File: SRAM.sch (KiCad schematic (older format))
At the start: 5 parts

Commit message: Merged 8254
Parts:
- gave numbers to parts that had none: 5
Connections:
- net BHE': now also U12.6 (I6); no longer U12.3 (I3)
- net M-IO': now also U12.7 (I7); no longer U12.4 (I4)
- net A19: now reaches U12.5 (I5)
- new net A17: U12.3 (I3)
- new net A18: U12.4 (I4)
- no-connect marks 10 -> 7
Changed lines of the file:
@@
 $Descr A4 11693 8268
 encoding utf-8
-Sheet 2 6
+Sheet 6 8
 Title ""
 Date ""
@@
 	3300 1700 3200 1700
 $Comp
-L Memory_RAM:CY7C199 U?
+L Memory_RAM:CY7C199 U13
 U 1 1 61BF2207
 P 3900 2600
-F 0 "U?" H 3900 3981 50  0000 C CNN
+F 0 "U13" H 3900 3981 50  0000 C CNN
 F 1 "CY7C199" H 3900 3890 50  0000 C CNN
 F 2 "" H 3900 2600 50  0001 C CNN
@@
 Wire Wire Line
 	3000 3500 3300 3500
-Wire Wire Line
-	1400 4000 1700 4000
 Text Notes 4600 1250 0    50   ~ 0
 Upper (ODD) Bank\n
 Text Notes 4550 7150 0    50   ~ 0
 Lower (Even) Bank\n
-$Comp
-L Logic_Programmable:PAL16L8 U?
-U 1 1 61C00AE8
-P 2200 4300
-F 0 "U?" H 2200 5181 50  0000 C CNN
-F 1 "PAL16L8" H 2200 5090 50  0000 C CNN
-F 2 "" H 2200 4300 50  0001 C CNN
-F 3 "" H 2200 4300 50  0001 C CNN
-	1    2200 4300
-	1    0    0    -1
-$EndComp
 Wire Wire Line
 	2700 3300 3300 3300
@@
 Wire Wire Line
 	1300 1400 1200 1400
-Wire Wire Line
-	1300 4100 1700 4100
-$Comp
-L power:GND #PWR?
+$Comp
+L power:GND #PWR0160
 U 1 1 61D25220
 P 3900 3800
-F 0 "#PWR?" H 3900 3550 50  0001 C CNN
+F 0 "#PWR0160" H 3900 3550 50  0001 C CNN
 F 1 "GND" H 3905 3627 50  0000 C CNN
 F 2 "" H 3900 3800 50  0001 C CNN
@@
 $EndComp
 $Comp
-L power:+5V #PWR?
+L power:+5V #PWR0161
 U 1 1 61D254C1
 P 3900 1400
-F 0 "#PWR?" H 3900 1250 50  0001 C CNN
+F 0 "#PWR0161" H 3900 1250 50  0001 C CNN
 F 1 "+5V" V 3915 1528 50  0000 L CNN
 F 2 "" H 3900 1400 50  0001 C CNN
@@
 $EndComp
 $Comp
-L power:+5V #PWR?
+L power:+5V #PWR0162
 U 1 1 61D260A2
 P 2200 3600
-F 0 "#PWR?" H 2200 3450 50  0001 C CNN
+F 0 "#PWR0162" H 2200 3450 50  0001 C CNN
 F 1 "+5V" V 2215 3728 50  0000 L CNN
 F 2 "" H 2200 3600 50  0001 C CNN
@@
 $EndComp
 $Comp
-L power:GND #PWR?
+L power:GND #PWR0163
 U 1 1 61D263BA
 P 2200 4900
-F 0 "#PWR?" H 2200 4650 50  0001 C CNN
+F 0 "#PWR0163" H 2200 4650 50  0001 C CNN
 F 1 "GND" H 2205 4727 50  0000 C CNN
 F 2 "" H 2200 4900 50  0001 C CNN
@@
 NoConn ~ 2700 4400
 NoConn ~ 2700 4500
-NoConn ~ 1700 4200
-NoConn ~ 1700 4300
-NoConn ~ 1700 4400
-NoConn ~ 1700 4500
 NoConn ~ 1700 4600
 NoConn ~ 1700 4700
@@
 	3300 4700 3200 4700
 $Comp
-L Memory_RAM:CY7C199 U?
+L Memory_RAM:CY7C199 U14
 U 1 1 61D93083
 P 3900 5600
-F 0 "U?" H 3900 6981 50  0000 C CNN
+F 0 "U14" H 3900 6981 50  0000 C CNN
 F 1 "CY7C199" H 3900 6890 50  0000 C CNN
 F 2 "" H 3900 5600 50  0001 C CNN
@@
 	3000 6500 3300 6500
 $Comp
-L power:GND #PWR?
+L power:GND #PWR0164
 U 1 1 61D930C9
 P 3900 6800
-F 0 "#PWR?" H 3900 6550 50  0001 C CNN
+F 0 "#PWR0164" H 3900 6550 50  0001 C CNN
 F 1 "GND" H 3905 6627 50  0000 C CNN
 F 2 "" H 3900 6800 50  0001 C CNN
@@
 $EndComp
 $Comp
-L power:+5V #PWR?
+L power:+5V #PWR0165
 U 1 1 61D930D3
 P 3900 4400
-F 0 "#PWR?" H 3900 4250 50  0001 C CNN
+F 0 "#PWR0165" H 3900 4250 50  0001 C CNN
 F 1 "+5V" V 3915 4528 50  0000 L CNN
 F 2 "" H 3900 4400 50  0001 C CNN
@@
 	5500 4700 5400 4700
 $Comp
-L Memory_RAM:CY7C199 U?
+L Memory_RAM:CY7C199 U16
 U 1 1 61DCF4EE
 P 6100 5600
-F 0 "U?" H 6100 6981 50  0000 C CNN
+F 0 "U16" H 6100 6981 50  0000 C CNN
 F 1 "CY7C199" H 6100 6890 50  0000 C CNN
 F 2 "" H 6100 5600 50  0001 C CNN
@@
 	4900 6300 5500 6300
 $Comp
-L power:GND #PWR?
+L power:GND #PWR0166
 U 1 1 61DCF52C
 P 6100 6800
-F 0 "#PWR?" H 6100 6550 50  0001 C CNN
+F 0 "#PWR0166" H 6100 6550 50  0001 C CNN
 F 1 "GND" H 6105 6627 50  0000 C CNN
 F 2 "" H 6100 6800 50  0001 C CNN
@@
 $EndComp
 $Comp
-L power:+5V #PWR?
+L power:+5V #PWR0167
 U 1 1 61DCF532
 P 6100 4400
-F 0 "#PWR?" H 6100 4250 50  0001 C CNN
+F 0 "#PWR0167" H 6100 4250 50  0001 C CNN
 F 1 "+5V" V 6115 4528 50  0000 L CNN
 F 2 "" H 6100 4400 50  0001 C CNN
@@
 	5500 1700 5400 1700
 $Comp
-L Memory_RAM:CY7C199 U?
+L Memory_RAM:CY7C199 U15
 U 1 1 61DD75B1
 P 6100 2600
-F 0 "U?" H 6100 3981 50  0000 C CNN
+F 0 "U15" H 6100 3981 50  0000 C CNN
 F 1 "CY7C199" H 6100 3890 50  0000 C CNN
 F 2 "" H 6100 2600 50  0001 C CNN
@@
 	4900 3300 5500 3300
 $Comp
-L power:GND #PWR?
+L power:GND #PWR0168
 U 1 1 61DD75EF
 P 6100 3800
-F 0 "#PWR?" H 6100 3550 50  0001 C CNN
+F 0 "#PWR0168" H 6100 3550 50  0001 C CNN
 F 1 "GND" H 6105 3627 50  0000 C CNN
 F 2 "" H 6100 3800 50  0001 C CNN
@@
 $EndComp
 $Comp
-L power:+5V #PWR?
+L power:+5V #PWR0169
 U 1 1 61DD75F5
 P 6100 1400
-F 0 "#PWR?" H 6100 1250 50  0001 C CNN
+F 0 "#PWR0169" H 6100 1250 50  0001 C CNN
 F 1 "+5V" V 6115 1528 50  0000 L CNN
 F 2 "" H 6100 1400 50  0001 C CNN
@@
 OE'
 Wire Wire Line
-	1300 1400 1300 4100
-Wire Wire Line
-	1400 1300 1400 4000
+	1300 1400 1300 4400
+Wire Wire Line
+	1400 1300 1400 4300
 Wire Wire Line
 	1200 1300 1400 1300
@@
 Text Label 6700 5400 0    50   ~ 0
 D7
+$Comp
+L Logic_Programmable:PAL16L8 U12
+U 1 1 61C00AE8
+P 2200 4300
+F 0 "U12" H 2200 5181 50  0000 C CNN
+F 1 "PAL16L8" H 2200 5090 50  0000 C CNN
+F 2 "" H 2200 4300 50  0001 C CNN
+F 3 "" H 2200 4300 50  0001 C CNN
+	1    2200 4300
+	1    0    0    -1
+$EndComp
+Wire Wire Line
+	1700 4000 1600 4000
+Wire Wire Line
+	1700 4100 1600 4100
+Wire Wire Line
+	1700 4200 1600 4200
+Entry Wire Line
+	1500 3900 1600 4000
+Entry Wire Line
+	1500 4000 1600 4100
+Entry Wire Line
+	1500 4100 1600 4200
+Text Label 1600 4000 0    50   ~ 0
+A17
+Text Label 1600 4100 0    50   ~ 0
+A18
+Text Label 1600 4200 0    50   ~ 0
+A19
+Wire Wire Line
+	1400 4300 1700 4300
+Wire Wire Line
+	1300 4400 1700 4400
+NoConn ~ 1700 4500
 Wire Bus Line
-	1500 1000 1500 3800
+	1500 1000 1500 4100
 Wire Bus Line
 	6900 1800 6900 4100

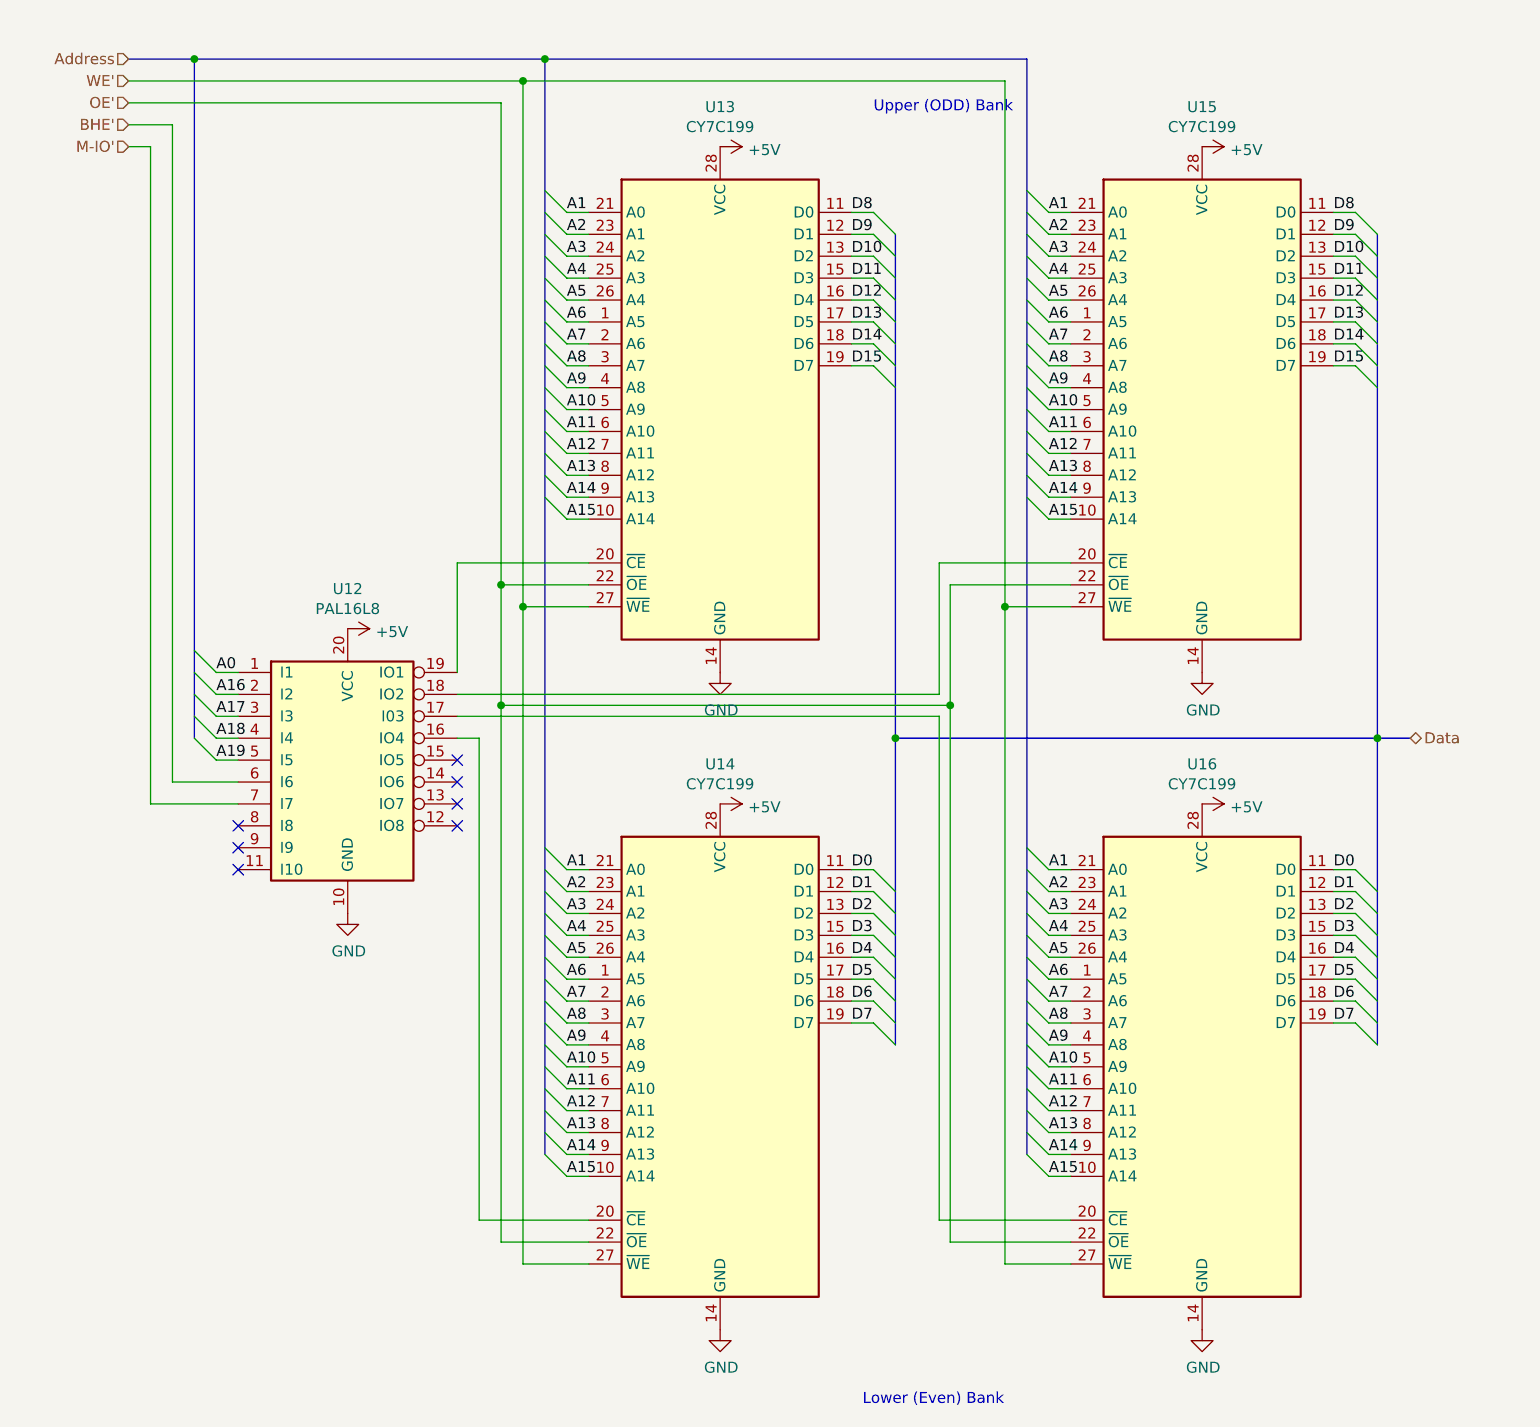
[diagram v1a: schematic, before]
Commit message: Integrated LCD.  Fixed issues with busses
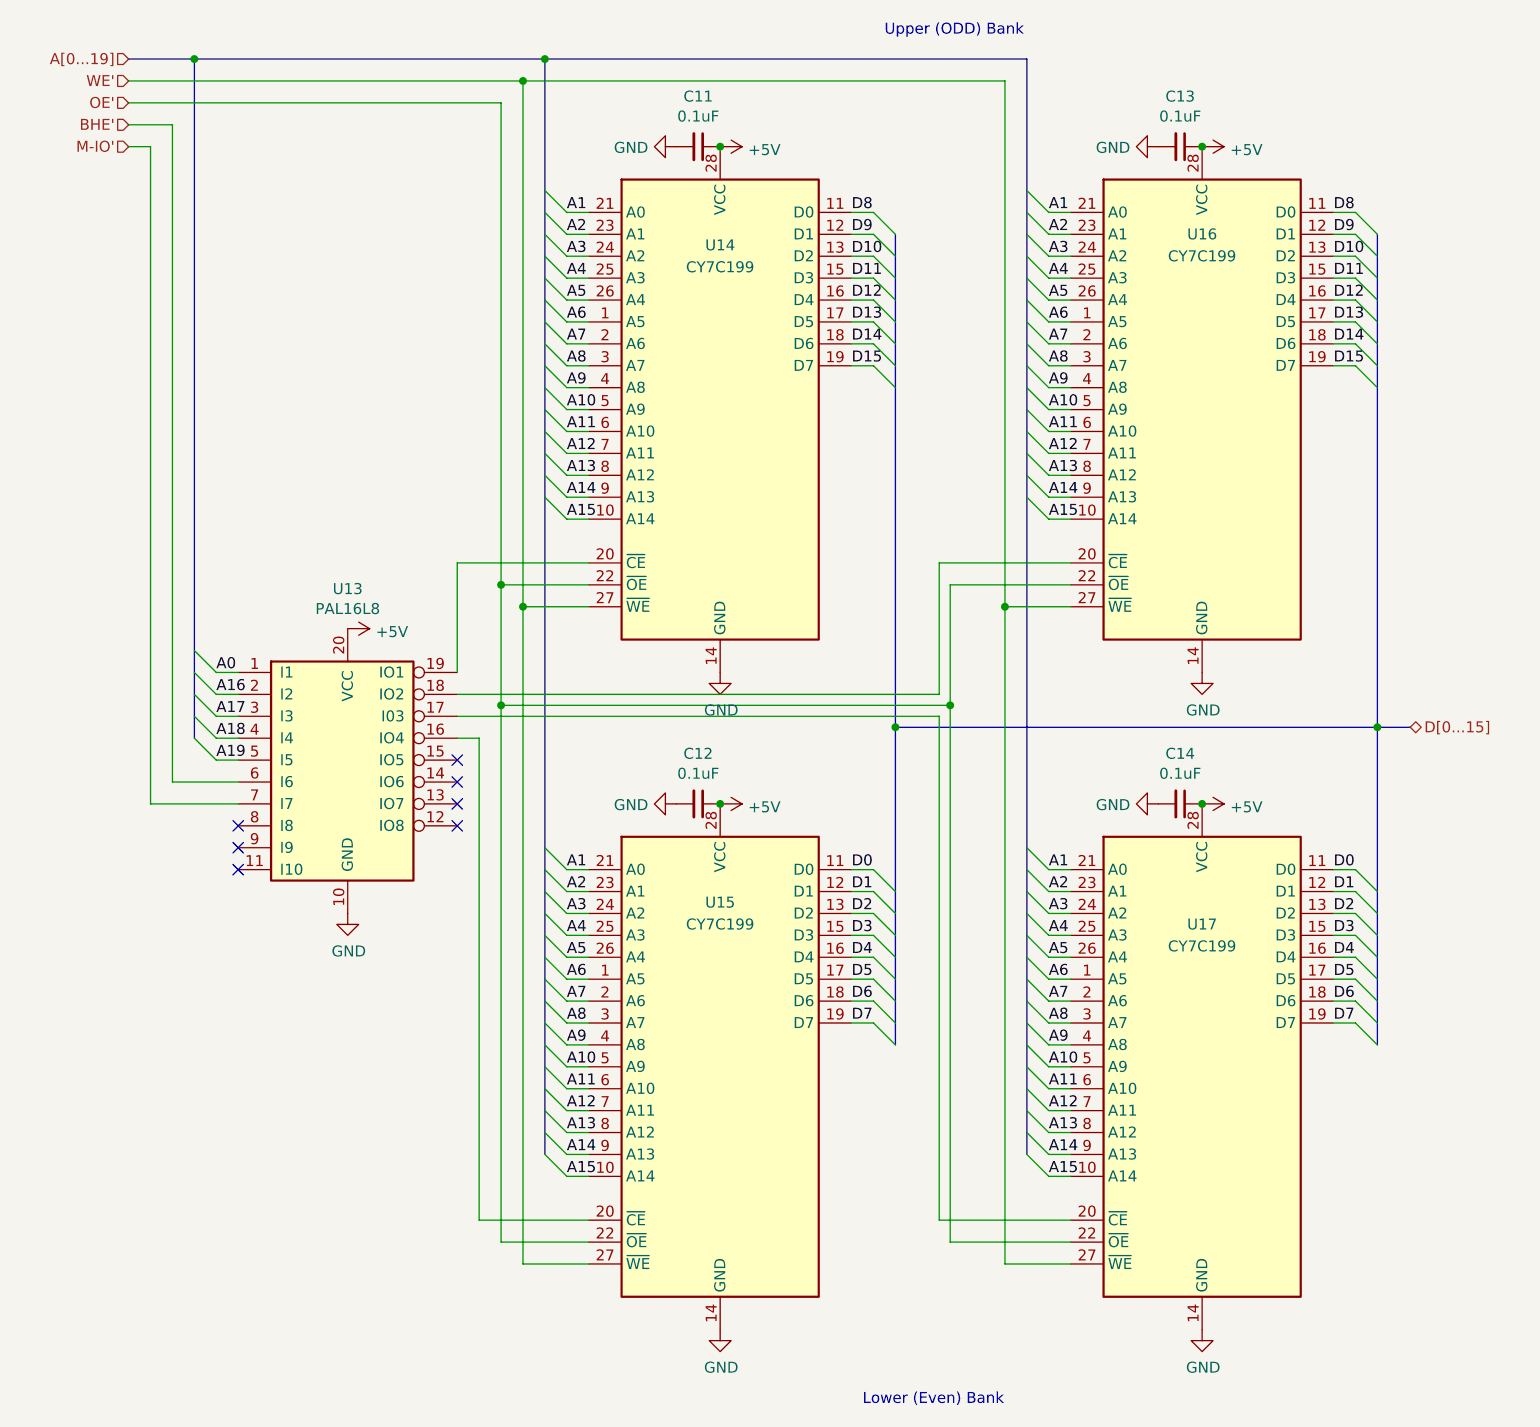
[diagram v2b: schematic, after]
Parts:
- added C11, C12, C13, C14: 0.1uF, symbol Device:C_Small
- renumbered U12 to U13, U13 to U14, U14 to U15, U15 to U16, U16 to U17
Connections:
- net +5V: now also C11.1, C12.1, C13.1, C14.1
- net GND: now also C11.2, C12.2, C13.2, C14.2
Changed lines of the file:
@@
 $Descr A4 11693 8268
 encoding utf-8
-Sheet 6 8
+Sheet 6 9
 Title ""
 Date ""
@@
 	3300 1700 3200 1700
 $Comp
-L Memory_RAM:CY7C199 U13
+L Memory_RAM:CY7C199 U14
 U 1 1 61BF2207
 P 3900 2600
-F 0 "U13" H 3900 3981 50  0000 C CNN
-F 1 "CY7C199" H 3900 3890 50  0000 C CNN
+F 0 "U14" H 3900 3350 50  0000 C CNN
+F 1 "CY7C199" H 3900 3250 50  0000 C CNN
 F 2 "" H 3900 2600 50  0001 C CNN
 F 3 "" H 3900 2600 50  0001 C CNN
@@
 Wire Wire Line
 	3000 3500 3300 3500
-Text Notes 4600 1250 0    50   ~ 0
+Text Notes 4650 900  0    50   ~ 0
 Upper (ODD) Bank\n
 Text Notes 4550 7150 0    50   ~ 0
@@
 	1200 1000 1500 1000
 Text HLabel 1200 1000 0    50   Input ~ 0
-Address
+A[0...19]
 Text HLabel 1200 1400 0    50   Input ~ 0
 M-IO'
@@
 	1300 1400 1200 1400
 $Comp
-L power:GND #PWR0160
+L power:GND #PWR074
 U 1 1 61D25220
 P 3900 3800
-F 0 "#PWR0160" H 3900 3550 50  0001 C CNN
+F 0 "#PWR074" H 3900 3550 50  0001 C CNN
 F 1 "GND" H 3905 3627 50  0000 C CNN
 F 2 "" H 3900 3800 50  0001 C CNN
@@
 $EndComp
 $Comp
-L power:+5V #PWR0161
+L power:+5V #PWR073
 U 1 1 61D254C1
 P 3900 1400
-F 0 "#PWR0161" H 3900 1250 50  0001 C CNN
+F 0 "#PWR073" H 3900 1250 50  0001 C CNN
 F 1 "+5V" V 3915 1528 50  0000 L CNN
 F 2 "" H 3900 1400 50  0001 C CNN
@@
 $EndComp
 $Comp
-L power:+5V #PWR0162
+L power:+5V #PWR069
 U 1 1 61D260A2
 P 2200 3600
-F 0 "#PWR0162" H 2200 3450 50  0001 C CNN
+F 0 "#PWR069" H 2200 3450 50  0001 C CNN
 F 1 "+5V" V 2215 3728 50  0000 L CNN
 F 2 "" H 2200 3600 50  0001 C CNN
@@
 $EndComp
 $Comp
-L power:GND #PWR0163
+L power:GND #PWR070
 U 1 1 61D263BA
 P 2200 4900
-F 0 "#PWR0163" H 2200 4650 50  0001 C CNN
+F 0 "#PWR070" H 2200 4650 50  0001 C CNN
 F 1 "GND" H 2205 4727 50  0000 C CNN
 F 2 "" H 2200 4900 50  0001 C CNN
@@
 	3300 4700 3200 4700
 $Comp
-L Memory_RAM:CY7C199 U14
+L Memory_RAM:CY7C199 U15
 U 1 1 61D93083
 P 3900 5600
-F 0 "U14" H 3900 6981 50  0000 C CNN
-F 1 "CY7C199" H 3900 6890 50  0000 C CNN
+F 0 "U15" H 3900 6350 50  0000 C CNN
+F 1 "CY7C199" H 3900 6250 50  0000 C CNN
 F 2 "" H 3900 5600 50  0001 C CNN
 F 3 "" H 3900 5600 50  0001 C CNN
@@
 	3000 6500 3300 6500
 $Comp
-L power:GND #PWR0164
+L power:GND #PWR076
 U 1 1 61D930C9
 P 3900 6800
-F 0 "#PWR0164" H 3900 6550 50  0001 C CNN
+F 0 "#PWR076" H 3900 6550 50  0001 C CNN
 F 1 "GND" H 3905 6627 50  0000 C CNN
 F 2 "" H 3900 6800 50  0001 C CNN
@@
 $EndComp
 $Comp
-L power:+5V #PWR0165
+L power:+5V #PWR075
 U 1 1 61D930D3
 P 3900 4400
-F 0 "#PWR0165" H 3900 4250 50  0001 C CNN
+F 0 "#PWR075" H 3900 4250 50  0001 C CNN
 F 1 "+5V" V 3915 4528 50  0000 L CNN
 F 2 "" H 3900 4400 50  0001 C CNN
@@
 Wire Wire Line
 	5500 4700 5400 4700
-$Comp
-L Memory_RAM:CY7C199 U16
-U 1 1 61DCF4EE
-P 6100 5600
-F 0 "U16" H 6100 6981 50  0000 C CNN
-F 1 "CY7C199" H 6100 6890 50  0000 C CNN
-F 2 "" H 6100 5600 50  0001 C CNN
-F 3 "" H 6100 5600 50  0001 C CNN
-	1    6100 5600
-	1    0    0    -1
-$EndComp
 Wire Wire Line
 	6700 4700 6800 4700
@@
 	4900 6300 5500 6300
 $Comp
-L power:GND #PWR0166
+L power:GND #PWR082
 U 1 1 61DCF52C
 P 6100 6800
-F 0 "#PWR0166" H 6100 6550 50  0001 C CNN
+F 0 "#PWR082" H 6100 6550 50  0001 C CNN
 F 1 "GND" H 6105 6627 50  0000 C CNN
 F 2 "" H 6100 6800 50  0001 C CNN
@@
 $EndComp
 $Comp
-L power:+5V #PWR0167
+L power:+5V #PWR081
 U 1 1 61DCF532
 P 6100 4400
-F 0 "#PWR0167" H 6100 4250 50  0001 C CNN
+F 0 "#PWR081" H 6100 4250 50  0001 C CNN
 F 1 "+5V" V 6115 4528 50  0000 L CNN
 F 2 "" H 6100 4400 50  0001 C CNN
@@
 	5500 1700 5400 1700
 $Comp
-L Memory_RAM:CY7C199 U15
+L Memory_RAM:CY7C199 U16
 U 1 1 61DD75B1
 P 6100 2600
-F 0 "U15" H 6100 3981 50  0000 C CNN
-F 1 "CY7C199" H 6100 3890 50  0000 C CNN
+F 0 "U16" H 6100 3400 50  0000 C CNN
+F 1 "CY7C199" H 6100 3300 50  0000 C CNN
 F 2 "" H 6100 2600 50  0001 C CNN
 F 3 "" H 6100 2600 50  0001 C CNN
@@
 	4900 3300 5500 3300
 $Comp
-L power:GND #PWR0168
+L power:GND #PWR080
 U 1 1 61DD75EF
 P 6100 3800
-F 0 "#PWR0168" H 6100 3550 50  0001 C CNN
+F 0 "#PWR080" H 6100 3550 50  0001 C CNN
 F 1 "GND" H 6105 3627 50  0000 C CNN
 F 2 "" H 6100 3800 50  0001 C CNN
@@
 $EndComp
 $Comp
-L power:+5V #PWR0169
+L power:+5V #PWR079
 U 1 1 61DD75F5
 P 6100 1400
-F 0 "#PWR0169" H 6100 1250 50  0001 C CNN
+F 0 "#PWR079" H 6100 1250 50  0001 C CNN
 F 1 "+5V" V 6115 1528 50  0000 L CNN
 F 2 "" H 6100 1400 50  0001 C CNN
@@
 Connection ~ 3100 1000
 Wire Bus Line
-	4700 4100 6900 4100
-Connection ~ 4700 4100
-Connection ~ 6900 4100
-Wire Bus Line
-	6900 4100 7050 4100
-Text HLabel 7050 4100 2    50   BiDi ~ 0
-Data
+	4700 4050 6900 4050
+Connection ~ 4700 4050
+Connection ~ 6900 4050
+Wire Bus Line
+	6900 4050 7050 4050
+Text HLabel 7050 4050 2    50   BiDi ~ 0
+D[0...15]
 Wire Wire Line
 	2700 3900 4900 3900
@@
 D7
 $Comp
-L Logic_Programmable:PAL16L8 U12
+L Logic_Programmable:PAL16L8 U13
 U 1 1 61C00AE8
 P 2200 4300
-F 0 "U12" H 2200 5181 50  0000 C CNN
+F 0 "U13" H 2200 5181 50  0000 C CNN
 F 1 "PAL16L8" H 2200 5090 50  0000 C CNN
 F 2 "" H 2200 4300 50  0001 C CNN
@@
 	1300 4400 1700 4400
 NoConn ~ 1700 4500
+$Comp
+L power:GND #PWR072
+U 1 1 61B7788D
+P 3700 4400
+F 0 "#PWR072" H 3700 4150 50  0001 C CNN
+F 1 "GND" V 3705 4272 50  0000 R CNN
+F 2 "" H 3700 4400 50  0001 C CNN
+F 3 "" H 3700 4400 50  0001 C CNN
+	1    3700 4400
+	0    1    1    0
+$EndComp
+$Comp
+L Device:C_Small C12
+U 1 1 61B929A4
+P 3800 4400
+F 0 "C12" V 3571 4400 50  0000 C CNN
+F 1 "0.1uF" V 3662 4400 50  0000 C CNN
+F 2 "" H 3800 4400 50  0001 C CNN
+F 3 "~" H 3800 4400 50  0001 C CNN
+	1    3800 4400
+	0    1    1    0
+$EndComp
+Connection ~ 3900 4400
+$Comp
+L Memory_RAM:CY7C199 U17
+U 1 1 61DCF4EE
+P 6100 5600
+F 0 "U17" H 6100 6250 50  0000 C CNN
+F 1 "CY7C199" H 6100 6150 50  0000 C CNN
+F 2 "" H 6100 5600 50  0001 C CNN
+F 3 "" H 6100 5600 50  0001 C CNN
+	1    6100 5600
+	1    0    0    -1
+$EndComp
+$Comp
+L Device:C_Small C14
+U 1 1 61BAF1F0
+P 6000 4400
+F 0 "C14" V 5771 4400 50  0000 C CNN
+F 1 "0.1uF" V 5862 4400 50  0000 C CNN
+F 2 "" H 6000 4400 50  0001 C CNN
+F 3 "~" H 6000 4400 50  0001 C CNN
+	1    6000 4400
+	0    1    1    0
+$EndComp
+Connection ~ 6100 4400
+$Comp
+L power:GND #PWR078
+U 1 1 61BAFEEF
+P 5900 4400
+F 0 "#PWR078" H 5900 4150 50  0001 C CNN
+F 1 "GND" V 5905 4272 50  0000 R CNN
+F 2 "" H 5900 4400 50  0001 C CNN
+F 3 "" H 5900 4400 50  0001 C CNN
+	1    5900 4400
+	0    1    1    0
+$EndComp
+$Comp
+L Device:C_Small C13
+U 1 1 61BB084F
+P 6000 1400
+F 0 "C13" V 5771 1400 50  0000 C CNN
+F 1 "0.1uF" V 5862 1400 50  0000 C CNN
+F 2 "" H 6000 1400 50  0001 C CNN
+F 3 "~" H 6000 1400 50  0001 C CNN
+	1    6000 1400
+	0    1    1    0
+$EndComp
+Connection ~ 6100 1400
+$Comp
+L Device:C_Small C11
+U 1 1 61BB16C0
+P 3800 1400
+F 0 "C11" V 3571 1400 50  0000 C CNN
+F 1 "0.1uF" V 3662 1400 50  0000 C CNN
+F 2 "" H 3800 1400 50  0001 C CNN
+F 3 "~" H 3800 1400 50  0001 C CNN
+	1    3800 1400
+	0    1    1    0
+$EndComp
+Connection ~ 3900 1400
+$Comp
+L power:GND #PWR071
+U 1 1 61BB1D2E
+P 3700 1400
+F 0 "#PWR071" H 3700 1150 50  0001 C CNN
+F 1 "GND" V 3705 1272 50  0000 R CNN
+F 2 "" H 3700 1400 50  0001 C CNN
+F 3 "" H 3700 1400 50  0001 C CNN
+	1    3700 1400
+	0    1    1    0
+$EndComp
+$Comp
+L power:GND #PWR077
+U 1 1 61BB20A9
+P 5900 1400
+F 0 "#PWR077" H 5900 1150 50  0001 C CNN
+F 1 "GND" V 5905 1272 50  0000 R CNN
+F 2 "" H 5900 1400 50  0001 C CNN
+F 3 "" H 5900 1400 50  0001 C CNN
+	1    5900 1400
+	0    1    1    0
+$EndComp
 Wire Bus Line
 	1500 1000 1500 4100
 Wire Bus Line
-	6900 1800 6900 4100
-Wire Bus Line
-	6900 4100 6900 5500
-Wire Bus Line
-	4700 4100 4700 5500
-Wire Bus Line
-	4700 1800 4700 4100
+	6900 1800 6900 4050
+Wire Bus Line
+	6900 4050 6900 5500
+Wire Bus Line
+	4700 4050 4700 5500
+Wire Bus Line
+	4700 1800 4700 4050
 Wire Bus Line
 	3100 1000 3100 6000
